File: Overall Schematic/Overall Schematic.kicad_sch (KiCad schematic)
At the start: 27 parts, among them U10 Encoder Breakout Board, U12 Spark MAX Motor Controller, U13 Max Breakout Board, U14 Encoder Breakout Board, U16 Spark MAX Motor Controller, U17 Max Breakout Board, U18 Encoder Breakout Board, U2 Jetson Nano, U20 Spark MAX Motor Controller, U21 Max Breakout Board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

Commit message: Completed Schematics
Only thing not included is a linear actuator and motor controller. Waiting on Mechanical to give us what they want to use
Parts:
- added 14.8V-5V1: Voltage Regulator, symbol New_Library:5V_CONVERTOR
- added BT1: 14.8 V, symbol Device:Battery_Cell
- added BT2: 14.8V, symbol Device:Battery_Cell
- added U28: E-STOP, symbol Lunabotics 2025-26:A22E-M-11
- added U29: Power Distribution Panel, symbol Lunabotics 2025-26:Power_Distribution_Panel
- added U30: Mini Power Distribution Panel, symbol Lunabotics 2025-26:Mini_Power_Distribution_Panel
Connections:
- net +5V: no longer names the net of U2.45 (5V)
- net +5V: now also U30.11 (5V_OUT), U30.12 (GRND)
- net 14.4V: no longer names the net of U6.4 (V+)
- net 14.4V: now also U29.34 (VCC_OUT_40A)
- removed net 14.5: U12.4 (V+), U16.4 (V+), U20.4 (V+), U5.4 (V+)
- removed net GND: U12.5 (V-), U16.5 (V-), U20.5 (V-), U5.5 (V-), U6.5 (V-)
- new net: BT1.1 (+), BT2.1 (+), U28.3 (24V)
- new net: BT1.2 (-), BT2.2 (-), U29.2 (GRND)
- new net: U12.4 (V+), U29.7 (VCC_OUT_40A)
- new net: U12.5 (V-), U29.8 (GRND)
- new net: 14.8V-5V1. (5V_6A_OUT), U30.1 (5V_IN)
- new net: 14.8V-5V1. (5V_6A_OUT), U30.2 (GRND)
- new net: 14.8V-5V1. (5V_6A_OUT), U29. (GRND) (x2)
- new net: U29.33 (GRND), U6.5 (V-)
- new net: U29.9 (VCC_OUT_40A), U5.4 (V+)
- new net: U29.10 (GRND), U5.5 (V-)
- new net: U28.2 (NC), U29.1 (14.8V_IN)
- new net: U20.4 (V+), U29.3 (VCC_OUT_40A)
- new net: U20.5 (V-), U29.4 (GRND)
- new net: U16.4 (V+), U29.5 (VCC_OUT_40A)
- new net: U16.5 (V-), U29.6 (GRND)
- no-connect marks 89 -> 90
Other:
- moved on the sheet: U1, U10, U11, U12, U13, U14, U15, U16, U17, U18, U19, U20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

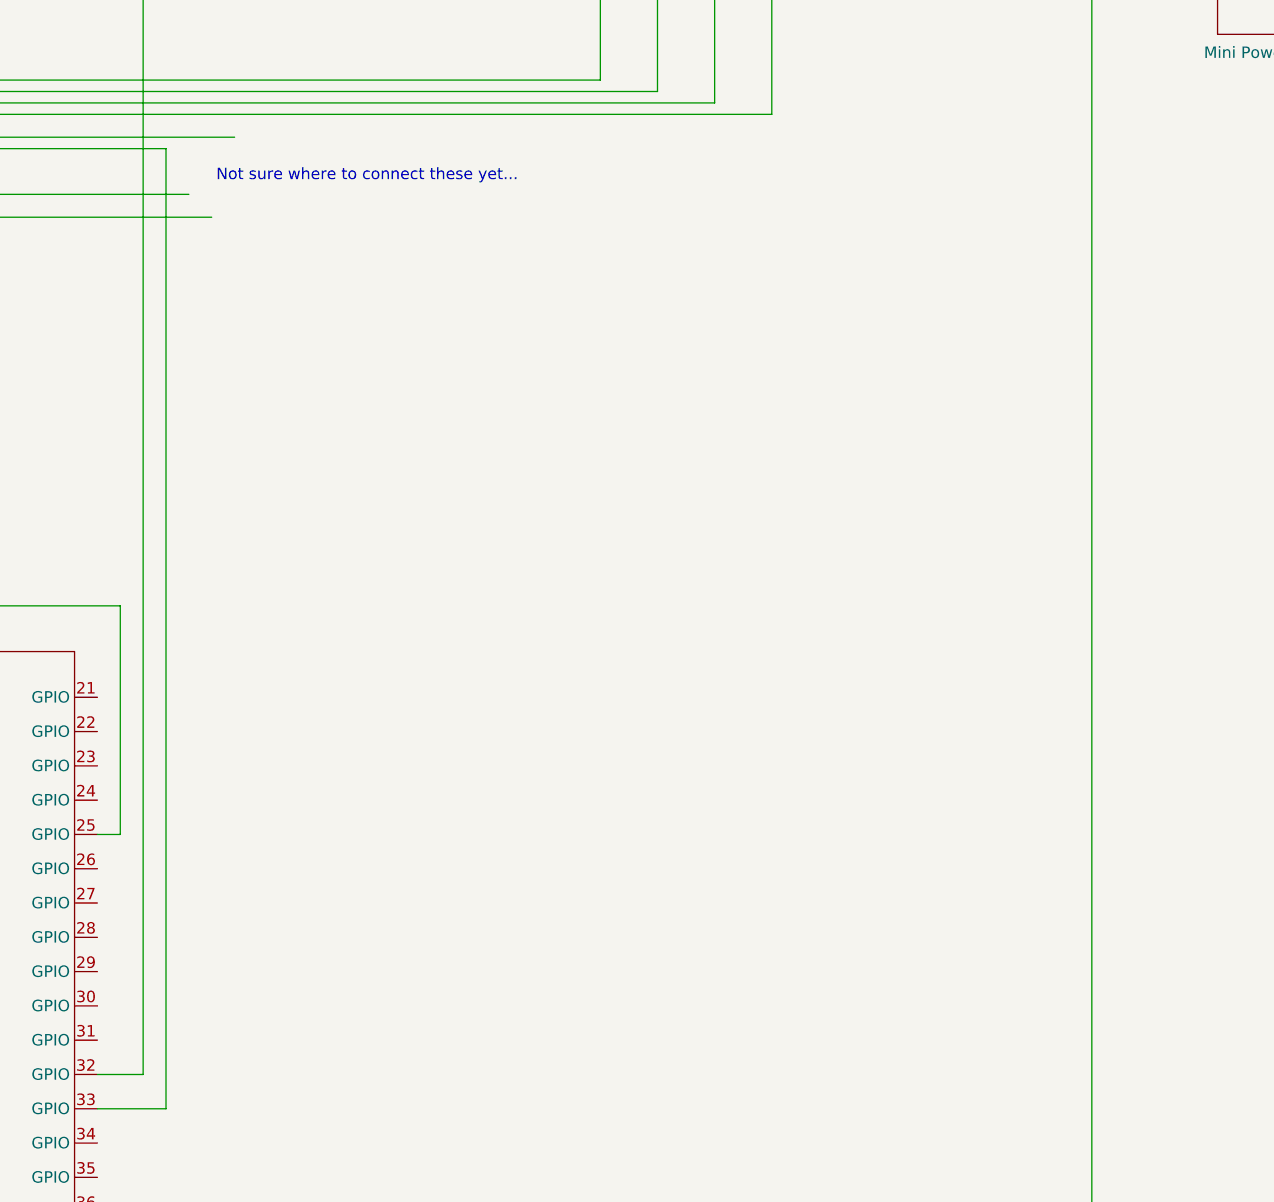
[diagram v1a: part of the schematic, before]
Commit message: Ported Linear Actuator to other schematics
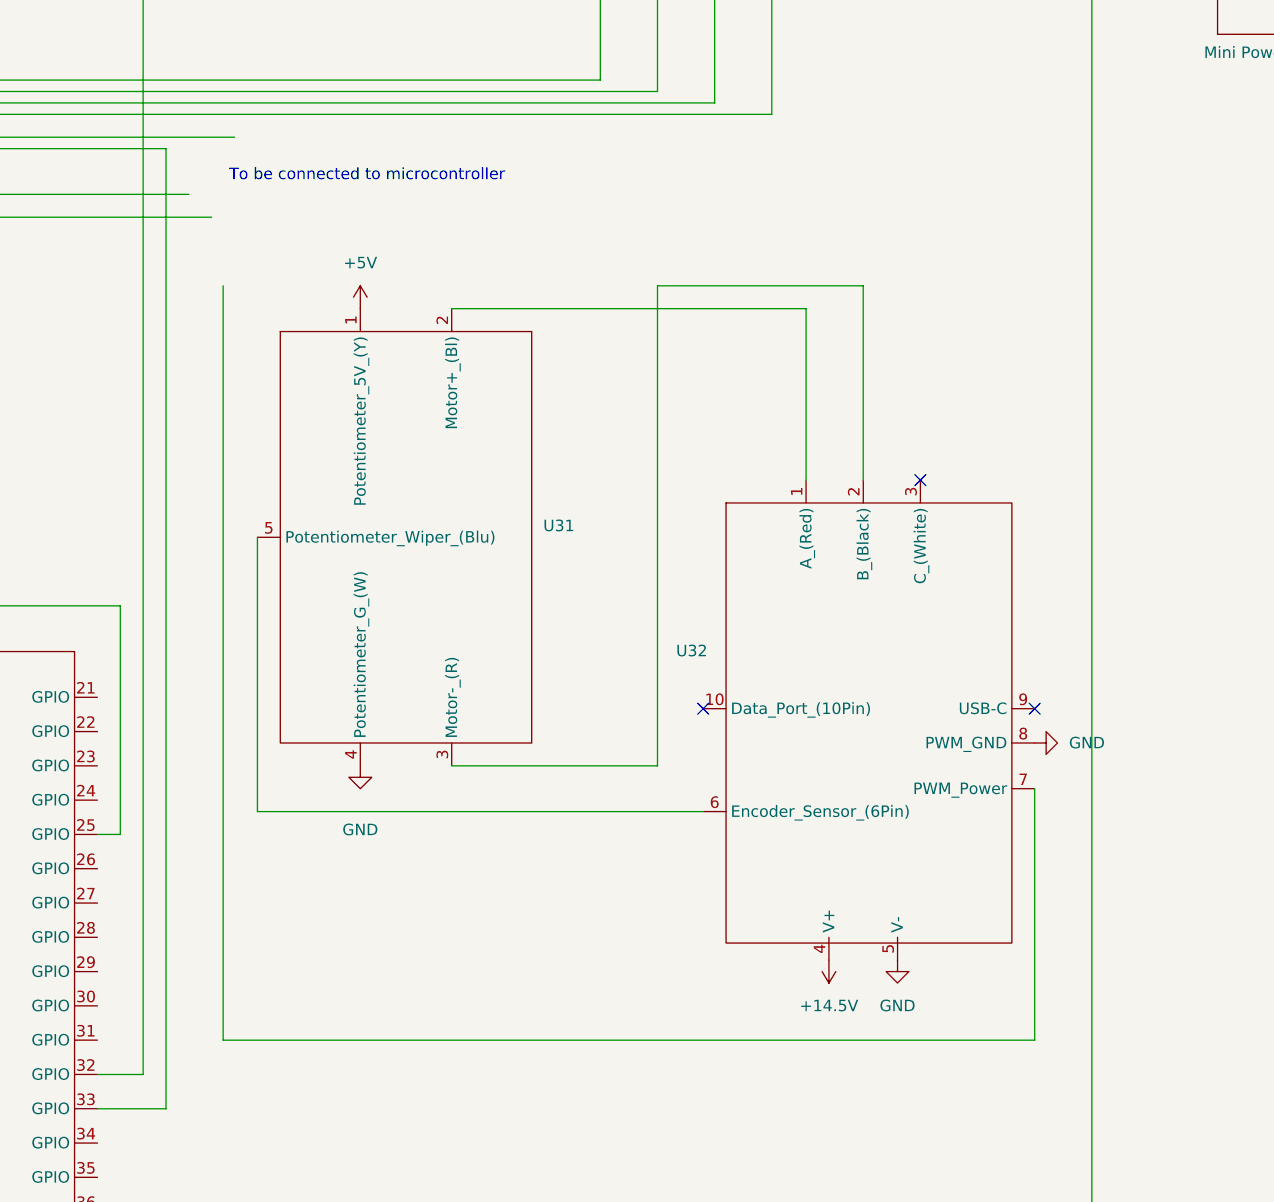
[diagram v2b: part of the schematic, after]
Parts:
- added U31: ~, symbol Lunabotics 2025-26:Feedback_Linear_Actuator
- added U32: ~, symbol Lunabotics 2025-26:Spark_MAX_Motor_Controller
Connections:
- net at U29. (GRND): no longer 14.8V-5V1. (5V_6A_OUT)
- new net: U31.2 (Motor+_(Bl)), U32.1 (A_(Red))
- new net: U31.3 (Motor-_(R)), U32.2 (B_(Black))
- new net: U31.5 (Potentiometer_Wiper_(Blu)), U32.6 (Encoder_Sensor_(6Pin))
- new net: 14.8V-5V1. (5V_6A_OUT), U29. (GRND)
- new net +14.5V: U32.4 (V+)
- new net +5V: U31.1 (Potentiometer_5V_(Y))
- new net GND: U31.4 (Potentiometer_G_(W)), U32.5 (V-), U32.8 (PWM_GND)
- no-connect marks 90 -> 93
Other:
- note added: "To be connected to microcontroller"
- note removed: "Not sure where to connect these yet..."

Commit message: Finalized Schematics with linear actuator and updated encoder
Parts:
- removed U10, U14, U18, U22, U9: Encoder Breakout Board, symbol Lunabotics 2025-26:Breakout_Board_Mag-Board
- removed U11, U15, U19, U23, U4: ~, symbol Lunabotics 2025-26:SRX_Mag_Encoder
- removed U13, U17, U21, U7, U8: Max Breakout Board, symbol Lunabotics 2025-26:Breakout_Board_Max-Board
- added U10, U4, U7, U8, U9: ~, symbol Lunabotics 2025-26:REV_Through_Bore_Encoder
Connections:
- net at U5.10 (Data_Port_(10Pin)): now also U8.1 (Encoder_Cable)
- net at U12.10 (Data_Port_(10Pin)): now also U10.1 (Encoder_Cable); no longer U5.7 (PWM_Power)
- net at U6.10 (Data_Port_(10Pin)): now also U9.1 (Encoder_Cable)
- net at U29. (GRND): no longer 14.8V-5V1. (5V_6A_OUT)
- net at U20.10 (Data_Port_(10Pin)): now also U4.1 (Encoder_Cable)
- net at U20.7 (PWM_Power): no longer U2.32 (GPIO)
- net at U2.33 (GPIO): no longer U16.7 (PWM_Power)
- net at U16.10 (Data_Port_(10Pin)): now also U7.1 (Encoder_Cable)
- new net: 14.8V-5V1. (5V_6A_OUT), U29. (GRND)
- no-connect marks 93 -> 28
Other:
- moved on the sheet: U12, U16, U20, U5, U6

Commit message: Updated Schematics & Library
Added Alternate Encoder to library and schematics, allows correct connection for Spark MAX to Neos. Also removed incorrect connection of linear actuator "encoder" to Spark MAX.
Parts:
- added U11, U13, U14, U15, U17: ~, symbol Lunabotics 2025-26:Rev_Alternate_Encoder_Adaptor
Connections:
- net at U32.6 (Encoder_Sensor_(6Pin)): no longer U31.5 (Potentiometer_Wiper_(Blu))
- net at U10.1 (Encoder_Cable): now also U17.2 (Encoder_Plug); no longer U12.10 (Data_Port_(10Pin))
- net at U6.10 (Data_Port_(10Pin)): now also U11.1 (Spark_MAX_Connection); no longer U9.1 (Encoder_Cable)
- net at U29. (GRND): no longer 14.8V-5V1. (5V_6A_OUT)
- net at U8.1 (Encoder_Cable): now also U14.2 (Encoder_Plug); no longer U5.10 (Data_Port_(10Pin))
- net at U4.1 (Encoder_Cable): now also U11.2 (Encoder_Plug); no longer U20.10 (Data_Port_(10Pin))
- net at U7.1 (Encoder_Cable): now also U13.2 (Encoder_Plug); no longer U16.10 (Data_Port_(10Pin))
- new net: U17.1 (Spark_MAX_Connection), U20.10 (Data_Port_(10Pin))
- new net: U12.10 (Data_Port_(10Pin)), U14.1 (Spark_MAX_Connection)
- new net: 14.8V-5V1. (5V_6A_OUT), U29. (GRND)
- new net: U15.1 (Spark_MAX_Connection), U16.10 (Data_Port_(10Pin))
- new net: U15.2 (Encoder_Plug), U9.1 (Encoder_Cable)
- new net: U13.1 (Spark_MAX_Connection), U5.10 (Data_Port_(10Pin))
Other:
- moved on the sheet: U4

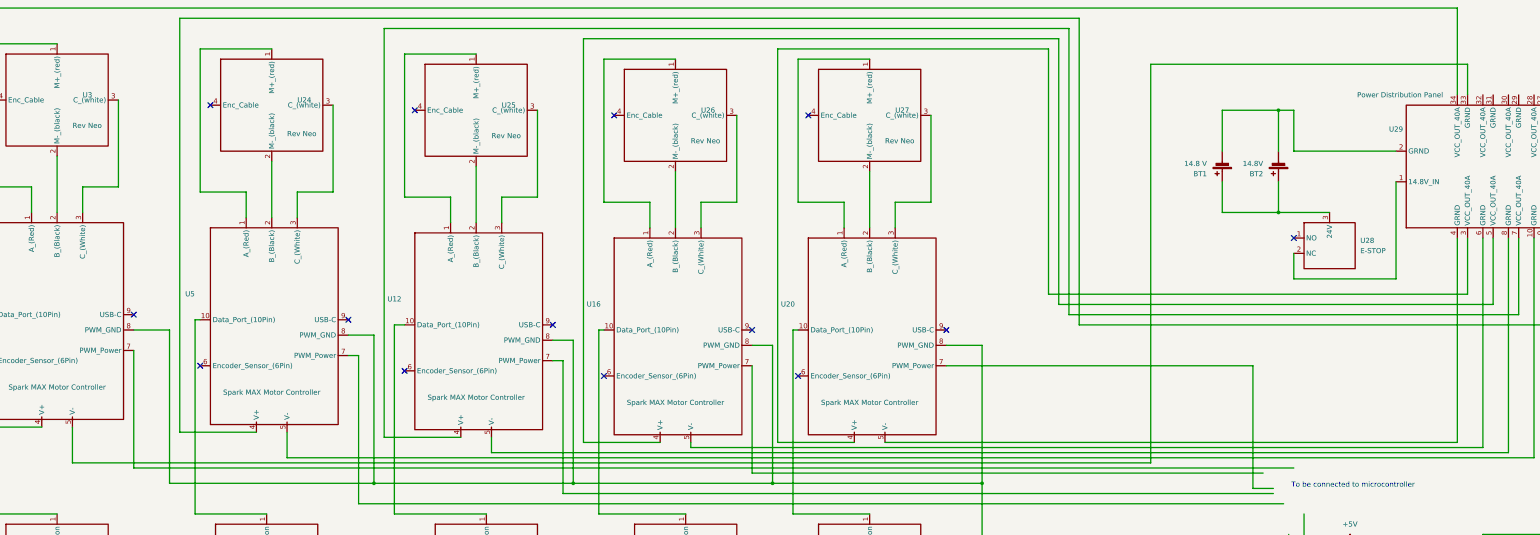
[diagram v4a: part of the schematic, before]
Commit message: Power System Changes
Added Power Meter and Power Meter Shunt to both power schematic and overall schematic
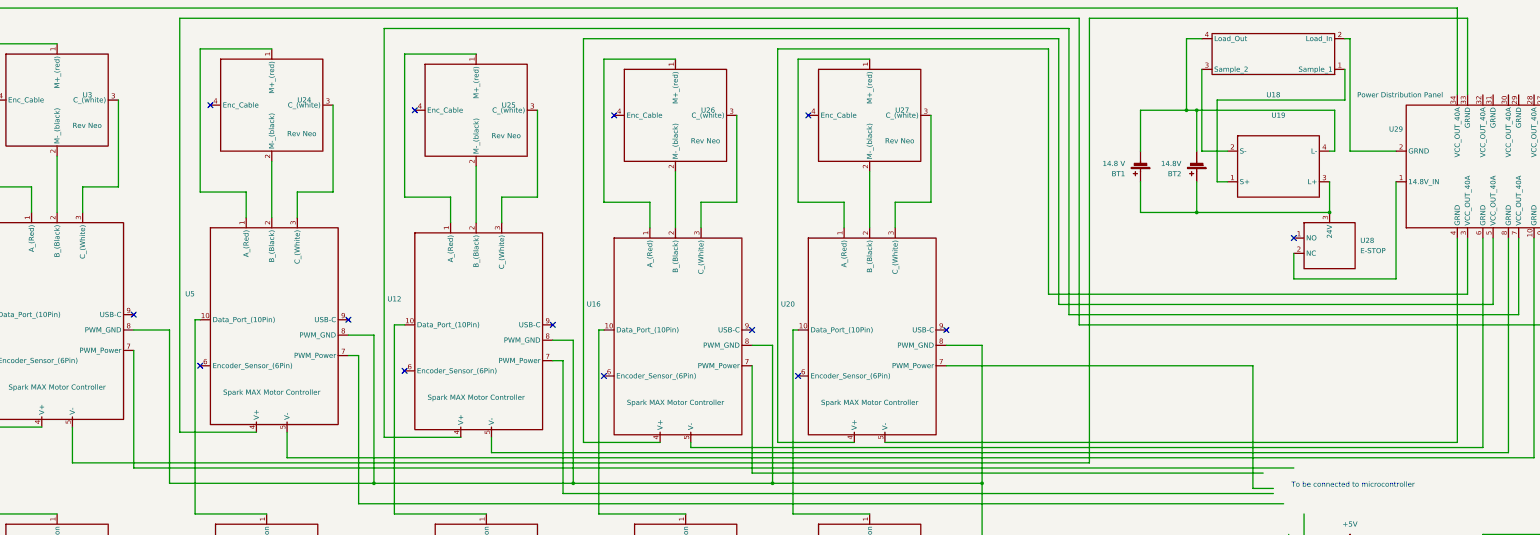
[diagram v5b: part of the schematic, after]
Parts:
- added U18: ~, symbol Lunabotics 2025-26:Power_Meter_Shunt
- added U19: ~, symbol Lunabotics 2025-26:Power_Meter
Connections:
- net at BT1.1 (+), BT2.1 (+), U28.3 (24V): now also U19.3 (L+)
- net at BT1.2 (-), BT2.2 (-): now also U18.4 (Load_Out), U19.4 (L-); no longer U29.2 (GRND)
- net at U29. (GRND): no longer 14.8V-5V1. (5V_6A_OUT)
- new net: 14.8V-5V1. (5V_6A_OUT), U29. (GRND)
- new net: U18.1 (Sample_1), U19.1 (S+)
- new net: U18.3 (Sample_2), U19.2 (S-)
- new net: U18.2 (Load_In), U29.2 (GRND)
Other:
- moved on the sheet: BT1, BT2
